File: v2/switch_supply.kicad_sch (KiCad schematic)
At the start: 9 parts

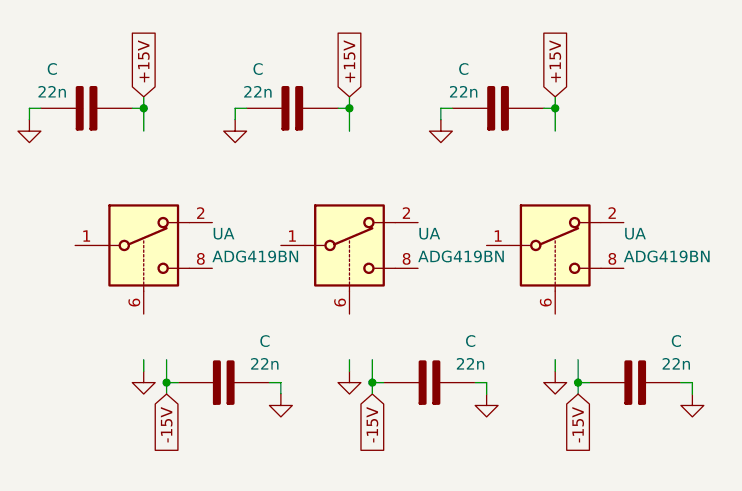
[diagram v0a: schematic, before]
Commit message: Added an unfinished pot stage
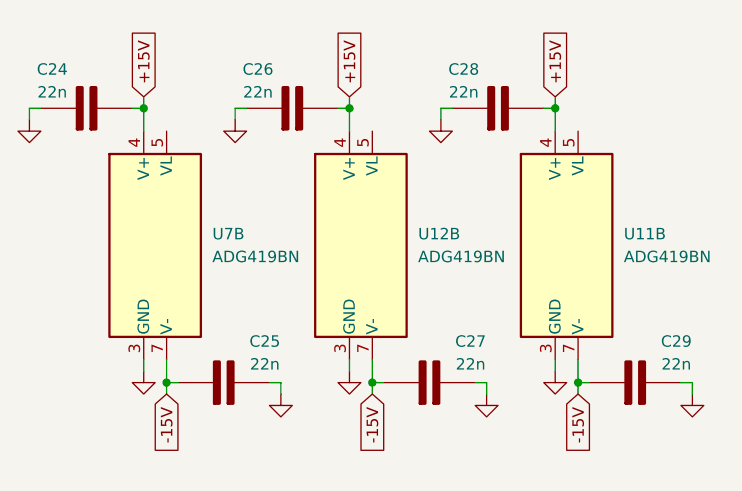
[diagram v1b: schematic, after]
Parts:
- renumbered C to C24, C to C25, C to C26, C to C27, C to C28, C to C29, U to U11, U to U12, U to U7
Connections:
- net +15V: now also U11.4 (V+), U12.4 (V+), U7.4 (V+)
- net -15V: now also U11.7 (V-), U12.7 (V-), U7.7 (V-)
- net GND: now also U11.3 (GND), U12.3 (GND), U7.3 (GND)
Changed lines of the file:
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@@
 		(dnp no)
 		(fields_autoplaced yes)
-		(property "Reference" "#PWR"
+		(property "Reference" "#PWR038"
 			(at 130.81 110.49 0)
 			(hide yes)
@@
 		(instances
 			(project "Charakterograf"
-				(path "/d7a5a570-e509-45ae-a7d3-ba88e6083368"
+				(path "/d7a5a570-e509-45ae-a7d3-ba88e6083368/0c87c16a-bedb-486e-a7c7-cc13502edb7f"
 					(reference "#PWR038")
 					(unit 1)
@@
 		(lib_id "Analog_Switch:ADG419BN")
 		(at 130.81 90.17 0)
-		(unit 1)
+		(unit 2)
 		(body_style 1)
 		(exclude_from_sim no)
@@
 		(dnp no)
 		(fields_autoplaced yes)
-		(property "Reference" "U"
+		(property "Reference" "U7"
 			(at 138.43 88.8999 0)
 			(show_name no)
@@
 					(unit 2)
 				)
+				(path "/d7a5a570-e509-45ae-a7d3-ba88e6083368/0c87c16a-bedb-486e-a7c7-cc13502edb7f"
+					(reference "U7")
+					(unit 2)
+				)
 			)
 		)
@@
 		(dnp no)
 		(fields_autoplaced yes)
-		(property "Reference" "#PWR"
+		(property "Reference" "#PWR040"
 			(at 140.97 82.55 0)
 			(hide yes)
@@
 		(instances
 			(project "Charakterograf"
-				(path "/d7a5a570-e509-45ae-a7d3-ba88e6083368"
+				(path "/d7a5a570-e509-45ae-a7d3-ba88e6083368/0c87c16a-bedb-486e-a7c7-cc13502edb7f"
 					(reference "#PWR040")
 					(unit 1)
@@
 		(in_pos_files yes)
 		(dnp no)
-		(property "Reference" "C"
+		(property "Reference" "C26"
 			(at 143.51 70.612 90)
 			(show_name no)
@@
 		(instances
 			(project "Charakterograf"
-				(path "/d7a5a570-e509-45ae-a7d3-ba88e6083368"
+				(path "/d7a5a570-e509-45ae-a7d3-ba88e6083368/0c87c16a-bedb-486e-a7c7-cc13502edb7f"
 					(reference "C26")
 					(unit 1)
@@
 		(dnp no)
 		(fields_autoplaced yes)
-		(property "Reference" "#PWR"
+		(property "Reference" "#PWR037"
 			(at 146.05 113.03 0)
 			(hide yes)
@@
 		(instances
 			(project "Charakterograf"
-				(path "/d7a5a570-e509-45ae-a7d3-ba88e6083368"
+				(path "/d7a5a570-e509-45ae-a7d3-ba88e6083368/0c87c16a-bedb-486e-a7c7-cc13502edb7f"
 					(reference "#PWR037")
 					(unit 1)
@@
 		(in_pos_files yes)
 		(dnp no)
-		(property "Reference" "C"
+		(property "Reference" "C28"
 			(at 166.37 70.612 90)
 			(show_name no)
@@
 		(instances
 			(project "Charakterograf"
-				(path "/d7a5a570-e509-45ae-a7d3-ba88e6083368"
+				(path "/d7a5a570-e509-45ae-a7d3-ba88e6083368/0c87c16a-bedb-486e-a7c7-cc13502edb7f"
 					(reference "C28")
 					(unit 1)
@@
 		(in_pos_files yes)
 		(dnp no)
-		(property "Reference" "C"
+		(property "Reference" "C25"
 			(at 144.272 100.838 90)
 			(show_name no)
@@
 		(instances
 			(project "Charakterograf"
-				(path "/d7a5a570-e509-45ae-a7d3-ba88e6083368"
+				(path "/d7a5a570-e509-45ae-a7d3-ba88e6083368/0c87c16a-bedb-486e-a7c7-cc13502edb7f"
 					(reference "C25")
 					(unit 1)
@@
 		(dnp no)
 		(fields_autoplaced yes)
-		(property "Reference" "#PWR"
+		(property "Reference" "#PWR042"
 			(at 168.91 113.03 0)
 			(hide yes)
@@
 		(instances
 			(project "Charakterograf"
-				(path "/d7a5a570-e509-45ae-a7d3-ba88e6083368"
+				(path "/d7a5a570-e509-45ae-a7d3-ba88e6083368/0c87c16a-bedb-486e-a7c7-cc13502edb7f"
 					(reference "#PWR042")
 					(unit 1)
@@
 		(in_pos_files yes)
 		(dnp no)
-		(property "Reference" "C"
+		(property "Reference" "C24"
 			(at 120.65 70.612 90)
 			(show_name no)
@@
 		(instances
 			(project "Charakterograf"
-				(path "/d7a5a570-e509-45ae-a7d3-ba88e6083368"
+				(path "/d7a5a570-e509-45ae-a7d3-ba88e6083368/0c87c16a-bedb-486e-a7c7-cc13502edb7f"
 					(reference "C24")
 					(unit 1)
@@
 		(dnp no)
 		(fields_autoplaced yes)
-		(property "Reference" "#PWR"
+		(property "Reference" "#PWR044"
 			(at 176.53 110.49 0)
 			(hide yes)
@@
 		(instances
 			(project "Charakterograf"
-				(path "/d7a5a570-e509-45ae-a7d3-ba88e6083368"
+				(path "/d7a5a570-e509-45ae-a7d3-ba88e6083368/0c87c16a-bedb-486e-a7c7-cc13502edb7f"
 					(reference "#PWR044")
 					(unit 1)
@@
 		(lib_id "Analog_Switch:ADG419BN")
 		(at 176.53 90.17 0)
-		(unit 1)
+		(unit 2)
 		(body_style 1)
 		(exclude_from_sim no)
@@
 		(dnp no)
 		(fields_autoplaced yes)
-		(property "Reference" "U"
+		(property "Reference" "U11"
 			(at 184.15 88.8999 0)
 			(show_name no)
@@
 			(project "Charakterograf"
 				(path "/d7a5a570-e509-45ae-a7d3-ba88e6083368"
+					(reference "U11")
+					(unit 2)
+				)
+				(path "/d7a5a570-e509-45ae-a7d3-ba88e6083368/0c87c16a-bedb-486e-a7c7-cc13502edb7f"
 					(reference "U11")
 					(unit 2)
@@
 		(in_pos_files yes)
 		(dnp no)
-		(property "Reference" "C"
+		(property "Reference" "C29"
 			(at 189.992 100.838 90)
 			(show_name no)
@@
 		(instances
 			(project "Charakterograf"
-				(path "/d7a5a570-e509-45ae-a7d3-ba88e6083368"
+				(path "/d7a5a570-e509-45ae-a7d3-ba88e6083368/0c87c16a-bedb-486e-a7c7-cc13502edb7f"
 					(reference "C29")
 					(unit 1)
@@
 		(dnp no)
 		(fields_autoplaced yes)
-		(property "Reference" "#PWR"
+		(property "Reference" "#PWR043"
 			(at 163.83 82.55 0)
 			(hide yes)
@@
 		(instances
 			(project "Charakterograf"
-				(path "/d7a5a570-e509-45ae-a7d3-ba88e6083368"
+				(path "/d7a5a570-e509-45ae-a7d3-ba88e6083368/0c87c16a-bedb-486e-a7c7-cc13502edb7f"
 					(reference "#PWR043")
 					(unit 1)
@@
 		(lib_id "Analog_Switch:ADG419BN")
 		(at 153.67 90.17 0)
-		(unit 1)
+		(unit 2)
 		(body_style 1)
 		(exclude_from_sim no)
@@
 		(dnp no)
 		(fields_autoplaced yes)
-		(property "Reference" "U"
+		(property "Reference" "U12"
 			(at 161.29 88.8999 0)
 			(show_name no)
@@
 			(project "Charakterograf"
 				(path "/d7a5a570-e509-45ae-a7d3-ba88e6083368"
+					(reference "U12")
+					(unit 2)
+				)
+				(path "/d7a5a570-e509-45ae-a7d3-ba88e6083368/0c87c16a-bedb-486e-a7c7-cc13502edb7f"
 					(reference "U12")
 					(unit 2)
@@
 		(in_pos_files yes)
 		(dnp no)
-		(property "Reference" "C"
+		(property "Reference" "C27"
 			(at 167.132 100.838 90)
 			(show_name no)
@@
 		(instances
 			(project "Charakterograf"
-				(path "/d7a5a570-e509-45ae-a7d3-ba88e6083368"
+				(path "/d7a5a570-e509-45ae-a7d3-ba88e6083368/0c87c16a-bedb-486e-a7c7-cc13502edb7f"
 					(reference "C27")
 					(unit 1)
@@
 		(dnp no)
 		(fields_autoplaced yes)
-		(property "Reference" "#PWR"
+		(property "Reference" "#PWR045"
 			(at 191.77 113.03 0)
 			(hide yes)
@@
 		(instances
 			(project "Charakterograf"
-				(path "/d7a5a570-e509-45ae-a7d3-ba88e6083368"
+				(path "/d7a5a570-e509-45ae-a7d3-ba88e6083368/0c87c16a-bedb-486e-a7c7-cc13502edb7f"
 					(reference "#PWR045")
 					(unit 1)
@@
 		(dnp no)
 		(fields_autoplaced yes)
-		(property "Reference" "#PWR"
+		(property "Reference" "#PWR041"
 			(at 153.67 110.49 0)
 			(hide yes)
@@
 		(instances
 			(project "Charakterograf"
-				(path "/d7a5a570-e509-45ae-a7d3-ba88e6083368"
+				(path "/d7a5a570-e509-45ae-a7d3-ba88e6083368/0c87c16a-bedb-486e-a7c7-cc13502edb7f"
 					(reference "#PWR041")
 					(unit 1)
@@
 		(dnp no)
 		(fields_autoplaced yes)
-		(property "Reference" "#PWR"
+		(property "Reference" "#PWR039"
 			(at 118.11 82.55 0)
 			(hide yes)
@@
 		(instances
 			(project "Charakterograf"
-				(path "/d7a5a570-e509-45ae-a7d3-ba88e6083368"
+				(path "/d7a5a570-e509-45ae-a7d3-ba88e6083368/0c87c16a-bedb-486e-a7c7-cc13502edb7f"
 					(reference "#PWR039")
 					(unit 1)

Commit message: Almostt finished everything, just finishing details
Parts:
- added C38, C39, C40: 100n, symbol custom:C_Basic
- C24, C25, C26, C27, C28, C29: value 22n -> 100n
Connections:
- net GND: now also C38., C39., C40.
- net 5V: now reaches U7.5 (VL)
- net 5V: now also U11.5 (VL), U12.5 (VL), C38., C39., C40.
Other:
- moved on the sheet: C24, C25, C26, C27, C28, C29, U11B, U12B, U7B

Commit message: Almost finished v2
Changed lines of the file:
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@@
 			(font
 				(size 1.27 1.27)
-				(thickness 0.254)
-				(bold yes)
+				(thickness 0.1588)
 			)
 			(justify left)
 		)
 		(property "Intersheetrefs" "${INTERSHEET_REFS}"
-			(at 82.55 39.9607 90)
+			(at 82.55 40.4367 90)
 			(hide yes)
 			(show_name no)
@@
 			(font
 				(size 1.27 1.27)
-				(thickness 0.254)
-				(bold yes)
+				(thickness 0.1588)
 			)
 			(justify left)
 		)
 		(property "Intersheetrefs" "${INTERSHEET_REFS}"
-			(at 114.3 39.9607 90)
+			(at 114.3 40.4367 90)
 			(hide yes)
 			(show_name no)
@@
 			(font
 				(size 1.27 1.27)
-				(thickness 0.254)
-				(bold yes)
+				(thickness 0.1588)
 			)
 			(justify left)
 		)
 		(property "Intersheetrefs" "${INTERSHEET_REFS}"
-			(at 146.05 39.9607 90)
+			(at 146.05 40.4367 90)
 			(hide yes)
 			(show_name no)
